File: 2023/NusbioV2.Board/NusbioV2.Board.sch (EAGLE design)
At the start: 27 parts

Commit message: Nsubio /2 v2 update
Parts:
- removed SW1: (no value), special:SW_DIP-4
- added I2C_OUT_1: (no value), pinhead:PINHD-1X4
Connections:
- removed net I2C_O2_1: I2C_OUT_2.1, SW1.1
- removed net I2C_O2_2: SW1.2
- removed net I2C_O2_3: I2C_OUT_2.2, SW1.3
- removed net I2C_O2_4: I2C_OUT_2.4, SW1.4
- net D0_SCLK: now also I2C_OUT_1.2, I2C_OUT_2.2
- net D2_MISO: now also I2C_OUT_1.1, I2C_OUT_2.1
- net GND: now also I2C_OUT_1.4, I2C_OUT_2.4
- net VCC_33: now also I2C_OUT_1.3
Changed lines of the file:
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@@
 <part name="JP_5V" library="pinhead" library_urn="urn:adsk.eagle:library:325" deviceset="PINHD-1X2" device="" package3d_urn="urn:adsk.eagle:package:22435/2"/>
 <part name="GND8" library="supply1" deviceset="GND" device=""/>
+<part name="I2C_OUT_1" library="pinhead" library_urn="urn:adsk.eagle:library:325" deviceset="PINHD-1X4" device="" package3d_urn="urn:adsk.eagle:package:22407/2"/>
+<part name="GND9" library="supply1" deviceset="GND" device=""/>
 <part name="I2C_PULL_UP_MODE" library="adafruit" deviceset="EG1218" device="S"/>
 <part name="R_PULL_UP_SCL_4K" library="adafruit" deviceset="R-US_" device="R1206"/>
 <part name="R_PULL_UP_SDA_4K" library="adafruit" deviceset="R-US_" device="R1206"/>
 <part name="I2C_OUT_2" library="pinhead" library_urn="urn:adsk.eagle:library:325" deviceset="PINHD-1X4" device="" package3d_urn="urn:adsk.eagle:package:22407/2"/>
+<part name="GND10" library="supply1" deviceset="GND" device=""/>
 <part name="I2C_DTA_CONN" library="adafruit" deviceset="EG1218" device="S"/>
 <part name="H1" library="holes" library_urn="urn:adsk.eagle:library:237" deviceset="MOUNT-PAD-ROUND" device="3.3" package3d_urn="urn:adsk.eagle:package:14283/1"/>
@@
 <part name="H3" library="holes" library_urn="urn:adsk.eagle:library:237" deviceset="MOUNT-PAD-ROUND" device="3.3" package3d_urn="urn:adsk.eagle:package:14283/1"/>
 <part name="H4" library="holes" library_urn="urn:adsk.eagle:library:237" deviceset="MOUNT-PAD-ROUND" device="3.3" package3d_urn="urn:adsk.eagle:package:14283/1"/>
-<part name="SW1" library="special" library_urn="urn:adsk.eagle:library:367" deviceset="SW_DIP-4" device="" package3d_urn="urn:adsk.eagle:package:26655/2"/>
 </parts>
 <sheets>
@@
 <attribute name="VALUE" x="-17.78" y="160.02" size="1.778" layer="96" rot="R90"/>
 </instance>
+<instance part="I2C_OUT_1" gate="A" x="-119.38" y="99.06" smashed="yes">
+<attribute name="NAME" x="-125.73" y="107.315" size="1.778" layer="95"/>
+<attribute name="VALUE" x="-125.73" y="91.44" size="1.778" layer="96"/>
+</instance>
+<instance part="GND9" gate="1" x="-142.24" y="96.52" smashed="yes" rot="R270">
+<attribute name="VALUE" x="-144.78" y="99.06" size="1.778" layer="96" rot="R90"/>
+</instance>
 <instance part="I2C_PULL_UP_MODE" gate="1" x="-119.38" y="71.12" smashed="yes" rot="R90">
 <attribute name="NAME" x="-104.775" y="67.31" size="1.778" layer="95" rot="R180"/>
@@
 <attribute name="VALUE" x="-125.73" y="111.76" size="1.778" layer="96"/>
 </instance>
+<instance part="GND10" gate="1" x="-144.78" y="116.84" smashed="yes" rot="R270">
+<attribute name="VALUE" x="-147.32" y="114.3" size="1.778" layer="96" rot="R90"/>
+</instance>
 <instance part="I2C_DTA_CONN" gate="1" x="-137.16" y="40.64" smashed="yes" rot="R90">
 <attribute name="NAME" x="-122.555" y="36.83" size="1.778" layer="95" rot="R180"/>
@@
 <attribute name="NAME" x="-83.566" y="180.9242" size="1.778" layer="95"/>
 <attribute name="VALUE" x="-83.566" y="177.8762" size="1.778" layer="96"/>
-</instance>
-<instance part="SW1" gate="A" x="-177.8" y="121.92" smashed="yes">
-<attribute name="NAME" x="-182.88" y="127.635" size="1.778" layer="95"/>
-<attribute name="VALUE" x="-182.88" y="111.76" size="1.778" layer="96"/>
 </instance>
 </instances>
@@
 <pinref part="GND8" gate="1" pin="GND"/>
 <wire x1="2.54" y1="157.48" x2="-12.7" y2="157.48" width="0.1524" layer="91"/>
+</segment>
+<segment>
+<pinref part="I2C_OUT_1" gate="A" pin="4"/>
+<pinref part="GND9" gate="1" pin="GND"/>
+<wire x1="-121.92" y1="96.52" x2="-139.7" y2="96.52" width="0.1524" layer="91"/>
+</segment>
+<segment>
+<pinref part="I2C_OUT_2" gate="A" pin="4"/>
+<pinref part="GND10" gate="1" pin="GND"/>
+<wire x1="-121.92" y1="116.84" x2="-142.24" y2="116.84" width="0.1524" layer="91"/>
 </segment>
 <segment>
@@
 </segment>
 <segment>
+<pinref part="I2C_OUT_1" gate="A" pin="3"/>
+<wire x1="-121.92" y1="99.06" x2="-134.62" y2="99.06" width="0.1524" layer="91"/>
+<label x="-137.16" y="99.06" size="1.778" layer="95"/>
+</segment>
+<segment>
 <pinref part="I2C_PULL_UP_MODE" gate="1" pin="P"/>
 <wire x1="-114.3" y1="73.66" x2="-104.14" y2="73.66" width="0.1524" layer="91"/>
@@
 <label x="-162.56" y="68.58" size="1.778" layer="95"/>
 </segment>
+<segment>
+<pinref part="I2C_OUT_2" gate="A" pin="2"/>
+<wire x1="-121.92" y1="121.92" x2="-144.78" y2="121.92" width="0.1524" layer="91"/>
+<label x="-142.24" y="121.92" size="1.778" layer="95"/>
+</segment>
+<segment>
+<pinref part="I2C_OUT_1" gate="A" pin="2"/>
+<wire x1="-121.92" y1="101.6" x2="-134.62" y2="101.6" width="0.1524" layer="91"/>
+<label x="-137.16" y="101.6" size="1.778" layer="95"/>
+</segment>
 </net>
 <net name="D1_MOSI" class="0">
@@
 <wire x1="-142.24" y1="40.64" x2="-160.02" y2="40.64" width="0.1524" layer="91"/>
 <label x="-162.56" y="43.18" size="1.778" layer="95"/>
+</segment>
+<segment>
+<pinref part="I2C_OUT_2" gate="A" pin="1"/>
+<wire x1="-121.92" y1="124.46" x2="-144.78" y2="124.46" width="0.1524" layer="91"/>
+<label x="-144.78" y="127" size="1.778" layer="95"/>
+</segment>
+<segment>
+<pinref part="I2C_OUT_1" gate="A" pin="1"/>
+<wire x1="-121.92" y1="104.14" x2="-132.08" y2="104.14" width="0.1524" layer="91"/>
+<label x="-137.16" y="106.68" size="1.778" layer="95"/>
 </segment>
 </net>
@@
 </segment>
 </net>
-<net name="I2C_O2_4" class="0">
-<segment>
-<pinref part="I2C_OUT_2" gate="A" pin="4"/>
-<wire x1="-121.92" y1="116.84" x2="-142.24" y2="116.84" width="0.1524" layer="91"/>
-<label x="-144.78" y="114.3" size="1.778" layer="95"/>
-</segment>
-<segment>
-<pinref part="SW1" gate="A" pin="4"/>
-<wire x1="-170.18" y1="124.46" x2="-160.02" y2="124.46" width="0.1524" layer="91"/>
-<label x="-170.18" y="124.46" size="1.778" layer="95"/>
-</segment>
-</net>
-<net name="I2C_O2_1" class="0">
-<segment>
-<pinref part="I2C_OUT_2" gate="A" pin="1"/>
-<wire x1="-121.92" y1="124.46" x2="-144.78" y2="124.46" width="0.1524" layer="91"/>
-<label x="-144.78" y="127" size="1.778" layer="95"/>
-</segment>
-<segment>
-<pinref part="SW1" gate="A" pin="1"/>
-<wire x1="-170.18" y1="116.84" x2="-157.48" y2="116.84" width="0.1524" layer="91"/>
-<label x="-167.64" y="114.3" size="1.778" layer="95"/>
-</segment>
-</net>
-<net name="I2C_O2_3" class="0">
-<segment>
-<pinref part="I2C_OUT_2" gate="A" pin="2"/>
-<wire x1="-121.92" y1="121.92" x2="-144.78" y2="121.92" width="0.1524" layer="91"/>
-<label x="-142.24" y="121.92" size="1.778" layer="95"/>
-</segment>
-<segment>
-<pinref part="SW1" gate="A" pin="3"/>
-<wire x1="-170.18" y1="121.92" x2="-157.48" y2="121.92" width="0.1524" layer="91"/>
-<label x="-170.18" y="121.92" size="1.778" layer="95"/>
-</segment>
-</net>
-<net name="I2C_O2_2" class="0">
-<segment>
-<pinref part="SW1" gate="A" pin="2"/>
-<wire x1="-170.18" y1="119.38" x2="-157.48" y2="119.38" width="0.1524" layer="91"/>
-<label x="-170.18" y="119.38" size="1.778" layer="95"/>
-</segment>
-</net>

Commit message: Nsubio /2 v2 update
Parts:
- removed JP_5V: (no value), pinhead:PINHD-1X2
- added VCC_5: (no value), adafruit:PINHD-1X1
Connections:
- net GND: no longer JP_5V.1
- net VCC_5: now also VCC_5.1; no longer JP_5V.2
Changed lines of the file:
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@@
 <part name="SPI_OUT_2" library="adafruit" deviceset="PINHD-1X10" device=""/>
 <part name="GND7" library="supply1" deviceset="GND" device=""/>
-<part name="JP_5V" library="pinhead" library_urn="urn:adsk.eagle:library:325" deviceset="PINHD-1X2" device="" package3d_urn="urn:adsk.eagle:package:22435/2"/>
-<part name="GND8" library="supply1" deviceset="GND" device=""/>
 <part name="I2C_OUT_1" library="pinhead" library_urn="urn:adsk.eagle:library:325" deviceset="PINHD-1X4" device="" package3d_urn="urn:adsk.eagle:package:22407/2"/>
 <part name="GND9" library="supply1" deviceset="GND" device=""/>
@@
 <part name="H3" library="holes" library_urn="urn:adsk.eagle:library:237" deviceset="MOUNT-PAD-ROUND" device="3.3" package3d_urn="urn:adsk.eagle:package:14283/1"/>
 <part name="H4" library="holes" library_urn="urn:adsk.eagle:library:237" deviceset="MOUNT-PAD-ROUND" device="3.3" package3d_urn="urn:adsk.eagle:package:14283/1"/>
+<part name="VCC_5" library="adafruit" deviceset="PINHD-1X1" device=""/>
 </parts>
 <sheets>
@@
 <attribute name="VALUE" x="-119.38" y="162.56" size="1.778" layer="96" rot="R90"/>
 </instance>
-<instance part="JP_5V" gate="G$1" x="5.08" y="154.94" smashed="yes">
-<attribute name="NAME" x="-1.27" y="160.655" size="1.778" layer="95"/>
-<attribute name="VALUE" x="-1.27" y="149.86" size="1.778" layer="96"/>
-</instance>
-<instance part="GND8" gate="1" x="-15.24" y="157.48" smashed="yes" rot="R270">
-<attribute name="VALUE" x="-17.78" y="160.02" size="1.778" layer="96" rot="R90"/>
-</instance>
 <instance part="I2C_OUT_1" gate="A" x="-119.38" y="99.06" smashed="yes">
 <attribute name="NAME" x="-125.73" y="107.315" size="1.778" layer="95"/>
@@
 <attribute name="NAME" x="-83.566" y="180.9242" size="1.778" layer="95"/>
 <attribute name="VALUE" x="-83.566" y="177.8762" size="1.778" layer="96"/>
+</instance>
+<instance part="VCC_5" gate="G$1" x="0" y="172.72" smashed="yes">
+<attribute name="NAME" x="-6.35" y="175.895" size="1.778" layer="95"/>
+<attribute name="VALUE" x="-6.35" y="167.64" size="1.778" layer="96"/>
 </instance>
 </instances>
@@
 <pinref part="GND7" gate="1" pin="GND"/>
 <wire x1="-81.28" y1="160.02" x2="-114.3" y2="160.02" width="0.1524" layer="91"/>
-</segment>
-<segment>
-<pinref part="JP_5V" gate="G$1" pin="1"/>
-<pinref part="GND8" gate="1" pin="GND"/>
-<wire x1="2.54" y1="157.48" x2="-12.7" y2="157.48" width="0.1524" layer="91"/>
 </segment>
 <segment>
@@
 </segment>
 <segment>
-<pinref part="JP_5V" gate="G$1" pin="2"/>
-<wire x1="2.54" y1="154.94" x2="-30.48" y2="154.94" width="0.1524" layer="91"/>
-</segment>
-</net>
+<pinref part="VCC_5" gate="G$1" pin="1"/>
+<wire x1="-2.54" y1="172.72" x2="-30.48" y2="172.72" width="0.1524" layer="91"/>
+<wire x1="-30.48" y1="172.72" x2="-30.48" y2="170.18" width="0.1524" layer="91"/>
+<label x="-27.94" y="170.18" size="1.778" layer="95"/>
+</segment>
+</net>

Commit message: Nsubio /2 v2 update
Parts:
- renumbered R_4K to R_2K
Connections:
- net VCC_33: now also LED_POWER.A
- net VCC_5: no longer LED_POWER.A
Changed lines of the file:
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@@
 <part name="LED_POWER" library="adafruit" deviceset="LED" device="SMT1206"/>
 <part name="GND1" library="supply1" deviceset="GND" device=""/>
-<part name="R_4K" library="adafruit" deviceset="R-US_" device="R1206"/>
+<part name="R_2K" library="adafruit" deviceset="R-US_" device="R1206"/>
 <part name="FT232H__SPI" library="pinhead" library_urn="urn:adsk.eagle:library:325" deviceset="PINHD-1X11" device="" package3d_urn="urn:adsk.eagle:package:22410/2"/>
 <part name="FT232H_GPIO" library="pinhead" library_urn="urn:adsk.eagle:library:325" deviceset="PINHD-1X11" device="" package3d_urn="urn:adsk.eagle:package:22410/2"/>
@@
 <attribute name="VALUE" x="-50.8" y="76.2" size="1.778" layer="96" rot="R90"/>
 </instance>
-<instance part="R_4K" gate="G$1" x="-27.94" y="73.66" smashed="yes">
+<instance part="R_2K" gate="G$1" x="-27.94" y="73.66" smashed="yes">
 <attribute name="NAME" x="-31.75" y="75.1586" size="1.778" layer="95"/>
 <attribute name="VALUE" x="-31.75" y="70.358" size="1.778" layer="96"/>
@@
 <net name="GND" class="0">
 <segment>
-<pinref part="R_4K" gate="G$1" pin="1"/>
+<pinref part="R_2K" gate="G$1" pin="1"/>
 <pinref part="GND1" gate="1" pin="GND"/>
 <wire x1="-33.02" y1="73.66" x2="-45.72" y2="73.66" width="0.1524" layer="91"/>
@@
 <label x="-144.78" y="119.38" size="1.778" layer="95"/>
 </segment>
+<segment>
+<pinref part="LED_POWER" gate="G$1" pin="A"/>
+<wire x1="7.62" y1="73.66" x2="25.4" y2="73.66" width="0.1524" layer="91"/>
+<label x="17.78" y="76.2" size="1.778" layer="95"/>
+</segment>
 </net>
 <net name="N$1" class="0">
 <segment>
 <pinref part="LED_POWER" gate="G$1" pin="C"/>
-<pinref part="R_4K" gate="G$1" pin="2"/>
+<pinref part="R_2K" gate="G$1" pin="2"/>
 <wire x1="0" y1="73.66" x2="-22.86" y2="73.66" width="0.1524" layer="91"/>
 </segment>
@@
 </segment>
 <segment>
-<pinref part="LED_POWER" gate="G$1" pin="A"/>
-<wire x1="7.62" y1="73.66" x2="25.4" y2="73.66" width="0.1524" layer="91"/>
-<label x="17.78" y="76.2" size="1.778" layer="95"/>
-</segment>
-<segment>

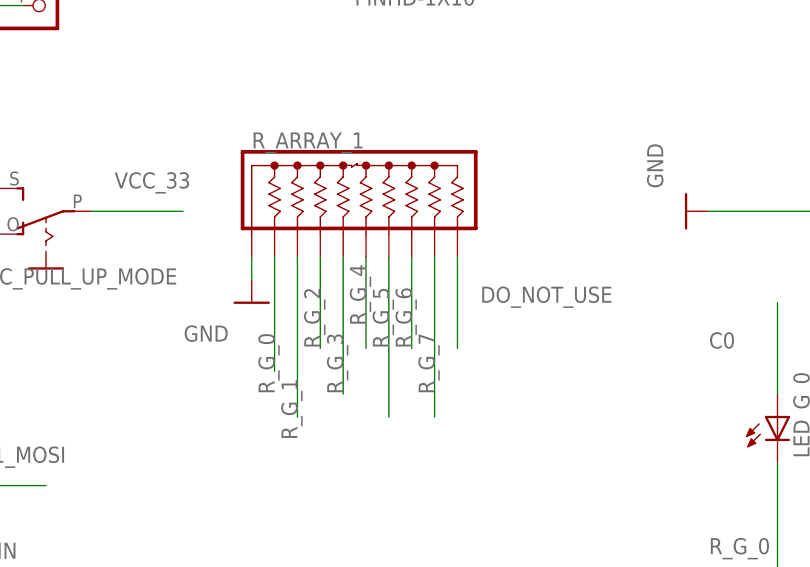
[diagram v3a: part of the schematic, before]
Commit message: Fix Nusbio gnd pin for gpios led resitor array
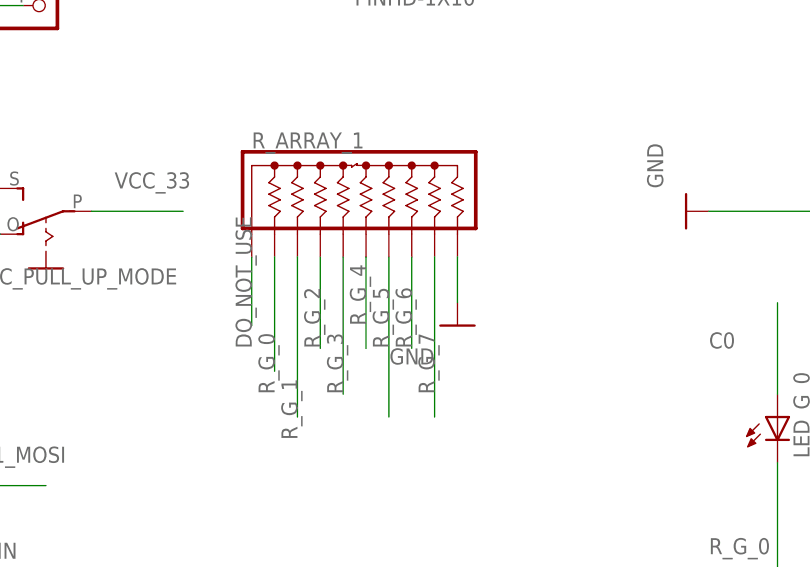
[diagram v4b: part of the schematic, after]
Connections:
- net DO_NOT_USE: now also R_ARRAY_1.1; no longer R_ARRAY_1.10
- net GND: now also R_ARRAY_1.10; no longer R_ARRAY_1.1
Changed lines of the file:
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@@
 <part name="GND5" library="supply1" deviceset="GND" device=""/>
 <part name="R_ARRAY_1" library="resistor-sip" deviceset="4610X" device=""/>
-<part name="GND6" library="supply1" deviceset="GND" device=""/>
 <part name="LED_G_0" library="adafruit" deviceset="LED" device="SMT1206"/>
 <part name="LED_G_1" library="adafruit" deviceset="LED" device="SMT1206"/>
@@
 <part name="H4" library="holes" library_urn="urn:adsk.eagle:library:237" deviceset="MOUNT-PAD-ROUND" device="3.3" package3d_urn="urn:adsk.eagle:package:14283/1"/>
 <part name="VCC_5" library="adafruit" deviceset="PINHD-1X1" device=""/>
+<part name="GND8" library="supply1" deviceset="GND" device=""/>
 </parts>
 <sheets>
@@
 <attribute name="VALUE" x="-81.28" y="80.645" size="1.778" layer="96"/>
 </instance>
-<instance part="GND6" gate="1" x="-96.52" y="63.5" smashed="yes">
-<attribute name="VALUE" x="-99.06" y="60.96" size="1.778" layer="96" rot="R180"/>
-</instance>
 <instance part="LED_G_0" gate="G$1" x="-38.1" y="50.8" smashed="yes">
 <attribute name="NAME" x="-34.544" y="46.228" size="1.778" layer="95" rot="R90"/>
@@
 <attribute name="NAME" x="-6.35" y="175.895" size="1.778" layer="95"/>
 <attribute name="VALUE" x="-6.35" y="167.64" size="1.778" layer="96"/>
+</instance>
+<instance part="GND8" gate="1" x="-73.66" y="60.96" smashed="yes">
+<attribute name="VALUE" x="-76.2" y="58.42" size="1.778" layer="96" rot="R180"/>
 </instance>
 </instances>
@@
 <pinref part="GND5" gate="1" pin="GND"/>
 <wire x1="27.94" y1="124.46" x2="7.62" y2="124.46" width="0.1524" layer="91"/>
-</segment>
-<segment>
-<pinref part="R_ARRAY_1" gate="G$1" pin="1"/>
-<pinref part="GND6" gate="1" pin="GND"/>
-<wire x1="-96.52" y1="68.58" x2="-96.52" y2="66.04" width="0.1524" layer="91"/>
 </segment>
 <segment>
@@
 <wire x1="-86.36" y1="180.34" x2="-88.9" y2="180.34" width="0.1524" layer="91"/>
 </segment>
+<segment>
+<pinref part="GND8" gate="1" pin="GND"/>
+<pinref part="R_ARRAY_1" gate="G$1" pin="10"/>
+<wire x1="-73.66" y1="63.5" x2="-73.66" y2="68.58" width="0.1524" layer="91"/>
+</segment>
 </net>
 <net name="VCC_33" class="0">
@@
 <wire x1="-38.1" y1="53.34" x2="-38.1" y2="63.5" width="0.1524" layer="91"/>
 <label x="-45.72" y="58.42" size="1.778" layer="95"/>
-</segment>
-</net>
-<net name="DO_NOT_USE" class="0">
-<segment>
-<pinref part="R_ARRAY_1" gate="G$1" pin="10"/>
-<wire x1="-73.66" y1="68.58" x2="-73.66" y2="58.42" width="0.1524" layer="91"/>
-<label x="-71.12" y="63.5" size="1.778" layer="95"/>
 </segment>
 </net>
@@
 </segment>
 </net>
+<net name="DO_NOT_USE" class="0">
+<segment>
+<pinref part="R_ARRAY_1" gate="G$1" pin="1"/>
+<wire x1="-96.52" y1="68.58" x2="-96.52" y2="60.96" width="0.1524" layer="91"/>
+<label x="-96.52" y="58.42" size="1.778" layer="95" rot="R90"/>
+</segment>
+</net>
